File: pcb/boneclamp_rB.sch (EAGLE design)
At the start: 65 parts, among them IC1 24C, U1 AD7656YSTZ, U2 AD5754RBREZ, U3 SN74ABT541BDW, U4 ADP3303ARZ-5, U5 ADP3303ARZ-5, U6 ADR431BRZ, U7 AD7682BCPZ

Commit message: More changes to circuit
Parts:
- removed U$26: LM1085, boneclamp:LM1085
- removed U$28: SCREW3, boneclamp:SCREW3
- added C21: 0.1uF, rcl:C-EUC0603
- added C25, C28: 10uF, rcl:C-USC1206
- added U8: TPS63700DRCT, ti-extended:TPS63700DRCT
- C19, C20: value 10uF -> 0.1uF; device rcl:C-USC1206 -> rcl:C-EUC0603
- U2: value AD5754RBREZ -> ADP3303ARZ-5; device analog-devices-01:AD5754RBREZ -> analog-devices-01:ADP3303ARZ-5
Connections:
- removed net +12V: C19.1, U$26.IN
- removed net -12V: U$28.P$3
- removed net PGND: U$28.P$2
- new net AVSS: C20.1, C21.1, C28.1, U2.OUT, U2.OUT_2
- new net N$26: C20.2, U2.NR
- net AGND: now also C19.2, C21.2, C25.2, C28.2, U2.GND
- net BB_5V: now also C19.1, C25.1, U2.IN, U2.IN_2, U2.~SD
- net DAC_A: no longer U2.VOUTA
- net DAC_B: no longer U2.VOUTB
- net DAC_C: no longer U2.VOUTC
- net DAC_D: no longer U2.VOUTD
- net DGND: no longer C19.2, C20.2, U$26.ADJ
- net DVCC: no longer U2.DVCC
- net N$24: no longer U2.REFIN/REFOUT
- net N$7: no longer U2.SDO
- net N$8: no longer U2.SDIN
- net VDD: no longer U2.AVDD
- net VDD_BB: no longer C20.1, U$26.OUT
- net VSS: no longer U2.AVSS
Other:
- moved on the sheet: C19, C20, JP4, SJ1, SJ2, SJ3, SJ4, U$42

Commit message: Worked a bit on the schematic
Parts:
- removed C23: 10uF, rcl:C-USC1206
- removed C24, C26, C27: 0.1uF, rcl:C-EUC0603
- removed JP5: (no value), jumper:JP2E
- removed JP6: (no value), jumper:JP1E
- removed TP5: TPB1,27, testpad:TPB1,27
- removed U3: SN74ABT541BDW, ti-extended:SN74ABT541BDW
- removed U6: ADR431BRZ, analog-devices-01:ADR431BRZ
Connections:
- removed net N$23: JP6.1
- removed net N$25: C26.1, U6.TP_2
- removed net VDD: C23.1, C24.1, U6.VIN
- removed net VREF_OUT: C27.1, JP5.3, JP6.2, TP5.TP, U6.VOUT
- net AGND: no longer C23.2, C24.2, C26.2, U6.GND
- net VREF_2.5V: no longer JP5.2
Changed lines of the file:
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@@
 <part name="U$1" library="adafruit" deviceset="BEAGLEBONE_OUTLINE" device=""/>
 <part name="U1" library="analog-devices-01" deviceset="AD7656YSTZ" device=""/>
-<part name="U3" library="ti-extended" deviceset="SN74ABT541BDW" device=""/>
 <part name="BCIO" library="adafruit" deviceset="F15-SHEILD" device=""/>
 <part name="JP1" library="jumper" deviceset="JP1E" device=""/>
@@
 <part name="SUPPLY1" library="supply2" deviceset="AGND" device=""/>
 <part name="DGND" library="supply2" deviceset="PE" device="" value="DGND"/>
-<part name="SUPPLY3" library="supply2" deviceset="0V" device="" value="PGND"/>
 <part name="SUPPLY4" library="supply2" deviceset="AGND" device=""/>
 <part name="SUPPLY5" library="supply2" deviceset="AGND" device=""/>
@@
 <part name="JP4" library="jumper" deviceset="JP1E" device=""/>
 <part name="U$45" library="boneclamp" deviceset="V_SIG" device=""/>
-<part name="U6" library="analog-devices-01" deviceset="ADR431BRZ" device=""/>
-<part name="C24" library="rcl" deviceset="C-EU" device="C0603" value="0.1uF"/>
-<part name="SUPPLY20" library="supply2" deviceset="AGND" device=""/>
-<part name="C26" library="rcl" deviceset="C-EU" device="C0603" value="0.1uF"/>
-<part name="C27" library="rcl" deviceset="C-EU" device="C0603" value="0.1uF"/>
-<part name="SUPPLY21" library="supply2" deviceset="AGND" device=""/>
 <part name="C5" library="rcl" deviceset="C-US" device="C1206" value="10uF"/>
 <part name="C8" library="rcl" deviceset="C-US" device="C1206" value="10uF"/>
 <part name="C10" library="rcl" deviceset="C-US" device="C1206" value="10uF"/>
 <part name="C13" library="rcl" deviceset="C-US" device="C1206" value="10uF"/>
-<part name="C23" library="rcl" deviceset="C-US" device="C1206" value="10uF"/>
-<part name="U$46" library="boneclamp" deviceset="V_SIG" device=""/>
-<part name="U$47" library="boneclamp" deviceset="V_SIG" device=""/>
-<part name="TP5" library="testpad" deviceset="TP" device="B1,27"/>
-<part name="JP5" library="jumper" deviceset="JP2E" device=""/>
-<part name="JP6" library="jumper" deviceset="JP1E" device=""/>
 <part name="U$42" library="analog-devices-02" deviceset="AD5686RARUZ" device=""/>
 <part name="U7" library="analog-devices-02" deviceset="AD7682BCPZ" device=""/>
@@
 <instances>
 <instance part="U$1" gate="G$1" x="-35.56" y="48.26"/>
-<instance part="U3" gate="A" x="48.26" y="53.34"/>
 <instance part="DGND2" gate="PE" x="2.54" y="-20.32"/>
 <instance part="SUPPLY8" gate="G$1" x="10.16" y="-20.32"/>
@@
 <instance part="SUPPLY1" gate="G$1" x="-81.28" y="45.72"/>
 <instance part="DGND" gate="PE" x="25.4" y="-33.02"/>
-<instance part="SUPPLY3" gate="0V" x="30.48" y="-58.42"/>
 <instance part="SUPPLY4" gate="G$1" x="-10.16" y="-22.86"/>
 <instance part="SUPPLY5" gate="G$1" x="0" y="-22.86"/>
@@
 </segment>
 </net>
-</nets>
-</sheet>
-<sheet>
-<description>REFERENCES</description>
-<plain>
-</plain>
-<instances>
-<instance part="U6" gate="A" x="0" y="0"/>
-<instance part="C24" gate="G$1" x="-48.26" y="-2.54"/>
-<instance part="SUPPLY20" gate="G$1" x="-48.26" y="-22.86"/>
-<instance part="C26" gate="G$1" x="-33.02" y="-2.54"/>
-<instance part="C27" gate="G$1" x="33.02" y="-2.54"/>
-<instance part="SUPPLY21" gate="G$1" x="33.02" y="-22.86"/>
-<instance part="C23" gate="G$1" x="-60.96" y="-2.54"/>
-<instance part="U$46" gate="G$1" x="116.84" y="0"/>
-<instance part="U$47" gate="G$1" x="-73.66" y="7.62" rot="R180"/>
-<instance part="TP5" gate="G$1" x="33.02" y="10.16"/>
-<instance part="JP5" gate="1" x="91.44" y="0" rot="R90"/>
-<instance part="JP6" gate="A" x="71.12" y="-2.54" rot="R90"/>
-</instances>
-<busses>
-</busses>
-<nets>
-<net name="AGND" class="0">
-<segment>
-<pinref part="U6" gate="A" pin="GND"/>
-<wire x1="-17.78" y1="-15.24" x2="-33.02" y2="-15.24" width="0.1524" layer="91"/>
-<wire x1="-33.02" y1="-15.24" x2="-48.26" y2="-15.24" width="0.1524" layer="91"/>
-<wire x1="-48.26" y1="-15.24" x2="-60.96" y2="-15.24" width="0.1524" layer="91"/>
-<wire x1="-60.96" y1="-15.24" x2="-60.96" y2="-7.62" width="0.1524" layer="91"/>
-<pinref part="C24" gate="G$1" pin="2"/>
-<wire x1="-48.26" y1="-7.62" x2="-48.26" y2="-15.24" width="0.1524" layer="91"/>
-<junction x="-48.26" y="-15.24"/>
-<wire x1="-48.26" y1="-15.24" x2="-48.26" y2="-20.32" width="0.1524" layer="91"/>
-<pinref part="SUPPLY20" gate="G$1" pin="AGND"/>
-<pinref part="C26" gate="G$1" pin="2"/>
-<wire x1="-33.02" y1="-7.62" x2="-33.02" y2="-15.24" width="0.1524" layer="91"/>
-<junction x="-33.02" y="-15.24"/>
-<pinref part="C23" gate="G$1" pin="2"/>
-</segment>
-<segment>
-<wire x1="33.02" y1="-7.62" x2="33.02" y2="-20.32" width="0.1524" layer="91"/>
-<pinref part="SUPPLY21" gate="G$1" pin="AGND"/>
-</segment>
-</net>
-<net name="VDD" class="0">
-<segment>
-<pinref part="U6" gate="A" pin="VIN"/>
-<wire x1="-17.78" y1="7.62" x2="-48.26" y2="7.62" width="0.1524" layer="91"/>
-<wire x1="-48.26" y1="7.62" x2="-60.96" y2="7.62" width="0.1524" layer="91"/>
-<wire x1="-60.96" y1="7.62" x2="-73.66" y2="7.62" width="0.1524" layer="91"/>
-<wire x1="-60.96" y1="0" x2="-60.96" y2="7.62" width="0.1524" layer="91"/>
-<junction x="-60.96" y="7.62"/>
-<pinref part="C24" gate="G$1" pin="1"/>
-<wire x1="-48.26" y1="0" x2="-48.26" y2="7.62" width="0.1524" layer="91"/>
-<junction x="-48.26" y="7.62"/>
-<pinref part="C23" gate="G$1" pin="1"/>
-<label x="-80.01" y="6.985" size="1.778" layer="95"/>
-</segment>
-</net>
-<net name="N$25" class="0">
-<segment>
-<pinref part="U6" gate="A" pin="TP_2"/>
-<wire x1="-17.78" y1="-5.08" x2="-22.86" y2="-5.08" width="0.1524" layer="91"/>
-<wire x1="-22.86" y1="-5.08" x2="-22.86" y2="2.54" width="0.1524" layer="91"/>
-<wire x1="-22.86" y1="2.54" x2="-33.02" y2="2.54" width="0.1524" layer="91"/>
-<pinref part="C26" gate="G$1" pin="1"/>
-<wire x1="-33.02" y1="2.54" x2="-33.02" y2="0" width="0.1524" layer="91"/>
-</segment>
-</net>
-<net name="VREF_2.5V" class="0">
-<segment>
-<pinref part="JP5" gate="1" pin="2"/>
-<wire x1="93.98" y1="0" x2="116.84" y2="0" width="0.1524" layer="91"/>
-<label x="118.11" y="-0.635" size="1.778" layer="95"/>
-</segment>
-</net>
-<net name="VREF_OUT" class="0">
-<segment>
-<pinref part="U6" gate="A" pin="VOUT"/>
-<wire x1="17.78" y1="7.62" x2="33.02" y2="7.62" width="0.1524" layer="91"/>
-<pinref part="C27" gate="G$1" pin="1"/>
-<wire x1="33.02" y1="0" x2="33.02" y2="7.62" width="0.1524" layer="91"/>
-<junction x="33.02" y="7.62"/>
-<pinref part="TP5" gate="G$1" pin="TP"/>
-<pinref part="JP5" gate="1" pin="3"/>
-<wire x1="93.98" y1="2.54" x2="101.6" y2="2.54" width="0.1524" layer="91"/>
-<wire x1="101.6" y1="2.54" x2="101.6" y2="7.62" width="0.1524" layer="91"/>
-<wire x1="101.6" y1="7.62" x2="73.66" y2="7.62" width="0.1524" layer="91"/>
-<pinref part="JP6" gate="A" pin="2"/>
-<wire x1="73.66" y1="7.62" x2="33.02" y2="7.62" width="0.1524" layer="91"/>
-<wire x1="73.66" y1="0" x2="73.66" y2="7.62" width="0.1524" layer="91"/>
-<junction x="73.66" y="7.62"/>
-</segment>
-</net>
-<net name="N$23" class="0">
-<segment>
-<pinref part="JP6" gate="A" pin="1"/>
-<wire x1="73.66" y1="-2.54" x2="73.66" y2="-35.56" width="0.1524" layer="91"/>
-<wire x1="73.66" y1="-35.56" x2="81.28" y2="-35.56" width="0.1524" layer="91"/>
-</segment>
-</net>

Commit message: Wired the DC-DC inverter
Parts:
- added C23: 10uF, rcl:C-EUC0805
- added C24: 22nF, rcl:C-EUC0805
- added C26: 0.1uF, rcl:C-EUC0805
- added C27: 4.7nF, rcl:C-EUC0805
- added C29: 10nF, rcl:C-EUC0805
- added C30, C31, C32, C33: 4.7uF, rcl:C-EUC0805
- added C34: 0.22uF, rcl:C-EUC0805
- added C35: 10pF, rcl:C-EUC0805
- added R12: 750, resistor:R-US_R0805
- added R13: 150k, resistor:R-US_R0805
- added R5: 100k, resistor:R-US_R0805
- added U$27: SCHOTTKY-DIODE-2, boneclamp:SCHOTTKY-DIODE-2
- added U$28: 4.7uH, boneclamp:L-US
- C15, C16, C17, C18: device rcl:C-EUC0603 -> rcl:C-EUC0805
- R1, R2, R3, R4: device rcl:R-US_R0603 -> rcl:R-US_R0805
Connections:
- removed net VDD_BB: U$1.VDD_5V@1, U$1.VDD_5V@2
- new net N$23: C26.1, R5.2, U8.EN, U8.VIN
- new net N$25: C27.1, U8.COMP
- new net N$27: U$27.A, U$28.1, U8.SW
- new net N$30: C35.1, R12.2, R13.1, U8.FB
- new net N$31: C34.1, R13.2, U8.VREF
- new net VDD_5V: C23.1, C24.1, R5.1, U$1.VDD_5V@1, U$1.VDD_5V@2, U8.IN
- new net _VSS: C29.1, C30.1, C31.1, C32.1, C33.1, C35.2, R12.1, U$27.C, U8.OUT
- net AGND: now also C23.2, C24.2, C26.2, C27.2, C29.2, C30.2, C31.2, C32.2, C33.2, C34.2, U$28.2, U8.EP, U8.GND, U8.PS_GND
- net BB_5V: no longer U$1.SYS_5V@1, U$1.SYS_5V@2
- net DAC_A: now also C15.1, R1.2, TP4.TP; no longer C18.1, R4.2, TP1.TP
- net DAC_B: now also C16.1, R2.2, TP3.TP; no longer C17.1, R3.2, TP2.TP
- net DAC_C: now also C17.1, R3.2, TP2.TP; no longer C16.1, R2.2, TP3.TP
- net DAC_D: now also C18.1, R4.2, TP1.TP; no longer C15.1, R1.2, TP4.TP

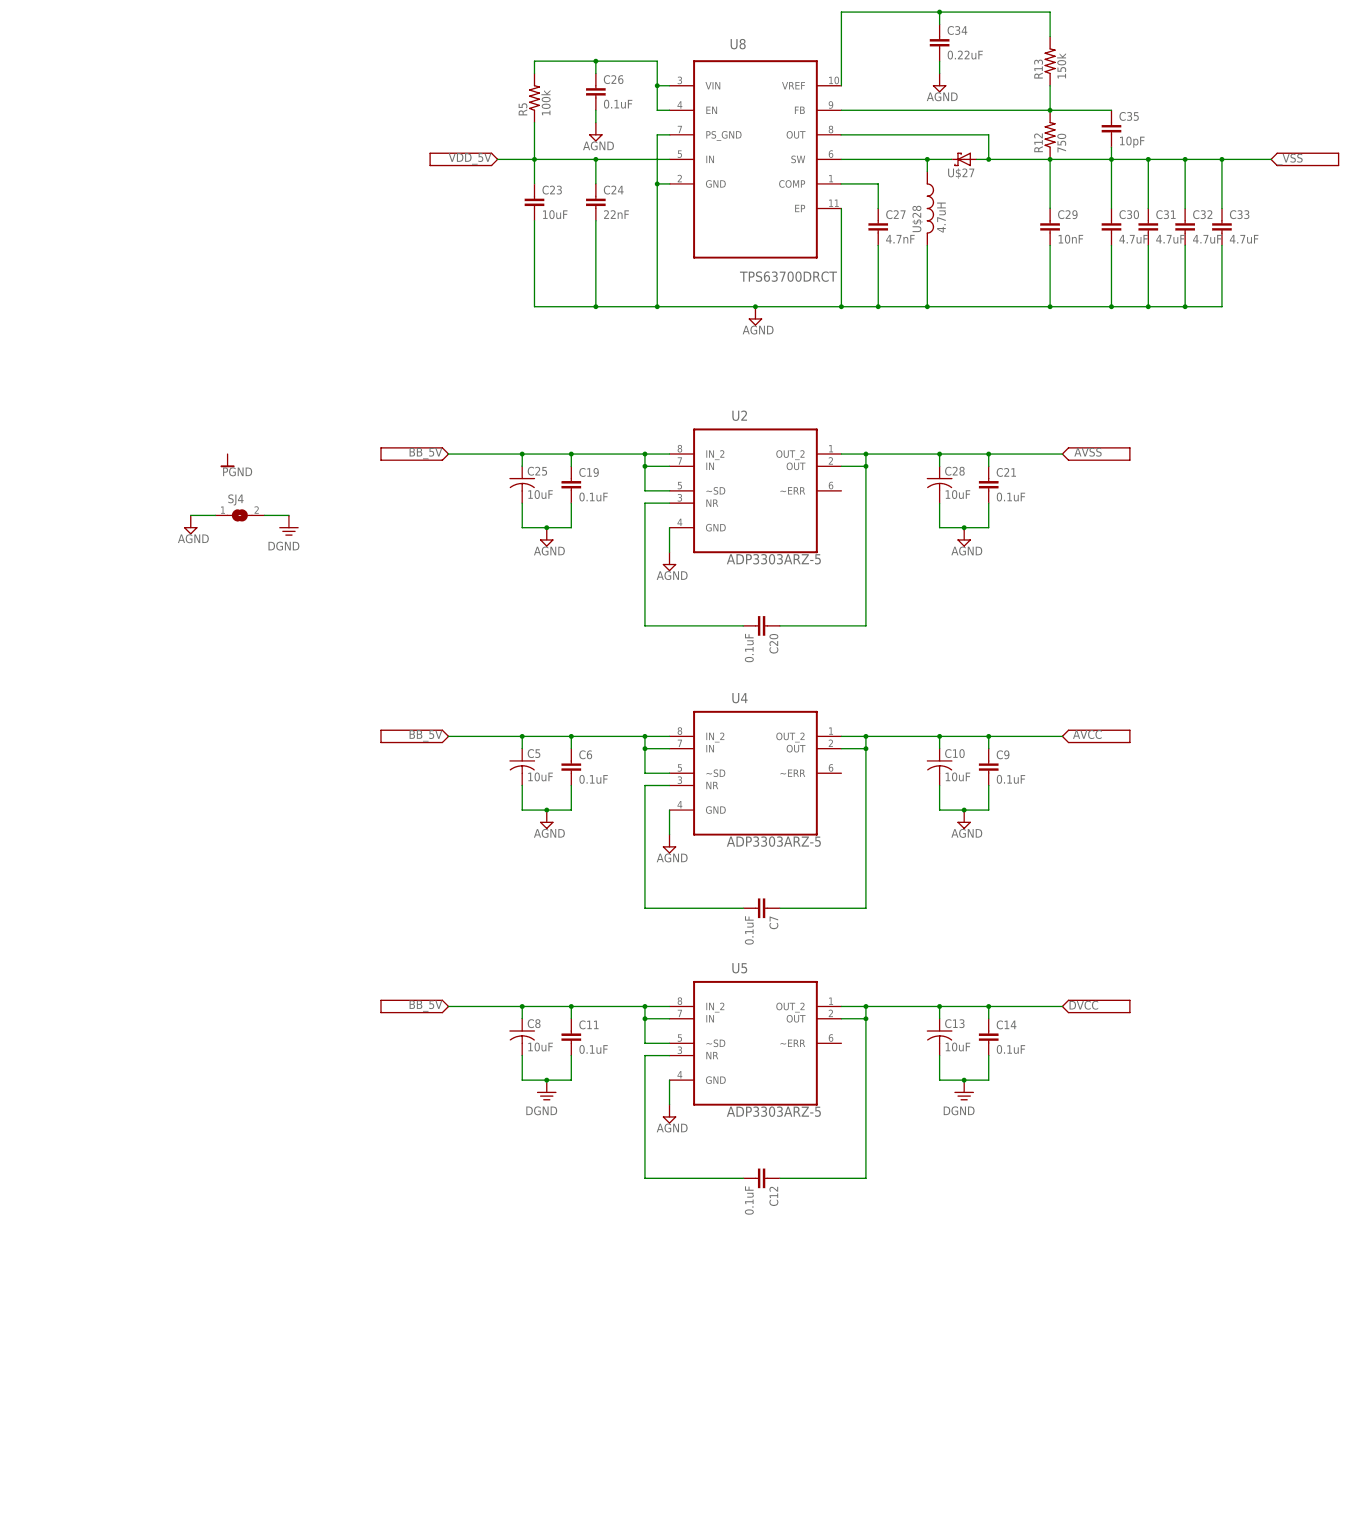
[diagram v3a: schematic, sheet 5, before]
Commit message: Added negative LDO regulator
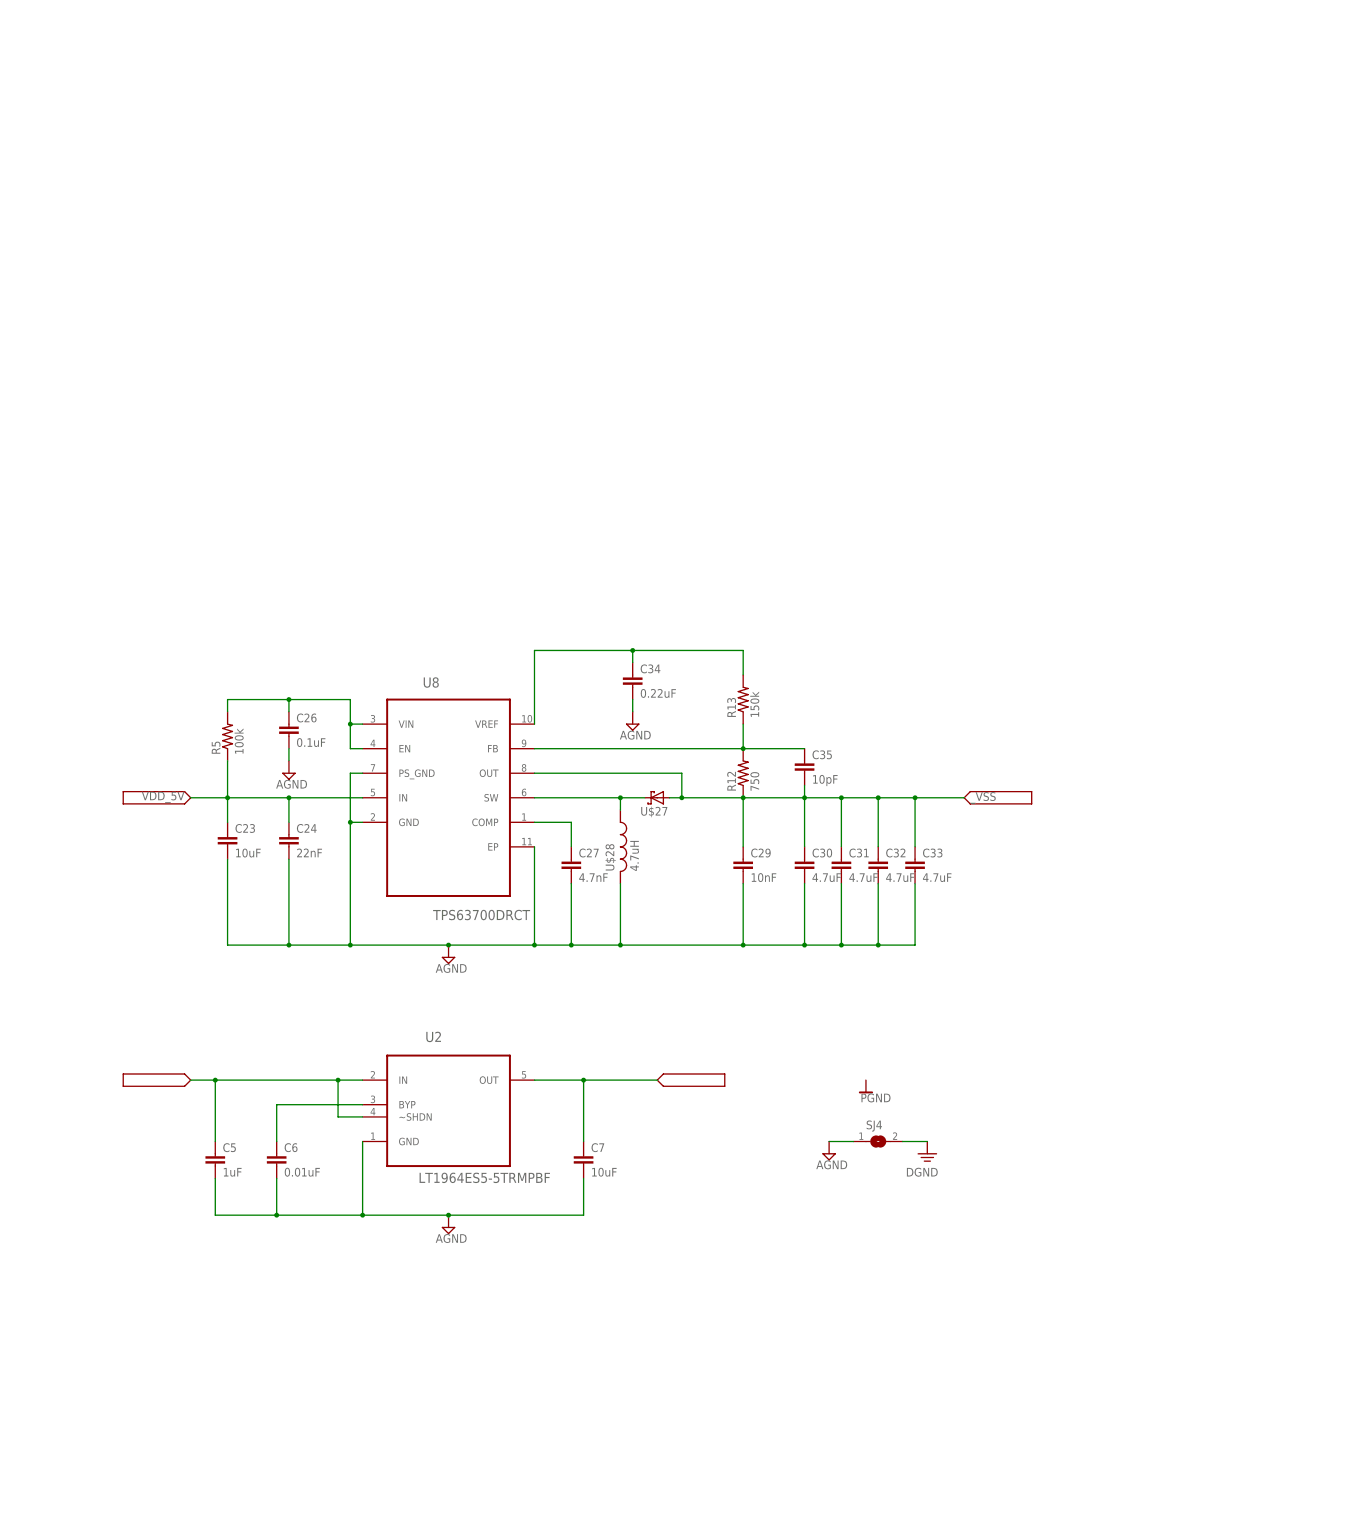
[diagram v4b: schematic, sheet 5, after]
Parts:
- removed C10, C13, C25, C28, C8: 10uF, rcl:C-USC1206
- removed C11, C12, C14, C19, C20, C21, C9: 0.1uF, rcl:C-EUC0603
- removed U4, U5: ADP3303ARZ-5, analog-devices-01:ADP3303ARZ-5
- C5: value 10uF -> 1uF; device rcl:C-USC1206 -> rcl:C-EUC0805
- C6: value 0.1uF -> 0.01uF; device rcl:C-EUC0603 -> rcl:C-EUC0805
- C7: value 0.1uF -> 10uF; device rcl:C-EUC0603 -> rcl:C-EUC0805
- U2: value ADP3303ARZ-5 -> LT1964ES5-5TRMPBF; device analog-devices-01:ADP3303ARZ-5 -> linear-extended-01:LT1964ES5-5TRMPBF
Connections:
- removed net AVCC: C10.1, C7.1, C9.1, U4.OUT, U4.OUT_2
- removed net AVSS: C20.1, C21.1, C28.1, U2.OUT, U2.OUT_2
- removed net BB_5V: C11.1, C19.1, C25.1, C5.1, C6.1, C8.1, U2.IN, U2.IN_2, U2.~SD, U4.IN, U4.IN_2, U4.~SD, U5.IN, U5.IN_2, U5.~SD
- removed net DVCC: C12.1, C13.1, C14.1, U5.OUT, U5.OUT_2
- removed net N$15: C12.2, U5.NR
- removed net N$26: C20.2, U2.NR
- new net VDD: U$42.VDD
- net AGND: now also C7.2; no longer C10.2, C19.2, C21.2, C25.2, C28.2, C9.2, U4.GND, U5.GND
- net DAC_A: now also U$42.VOUTA
- net DAC_B: now also U$42.VOUTB
- net DAC_C: now also U$42.VOUTC
- net DAC_D: now also U$42.VOUTD
- net DGND: no longer C11.2, C13.2, C14.2, C8.2
- net N$16: now also C6.1, U2.BYP; no longer C7.2, U4.NR
- net N$24: now also U$42.VREF
- net N$7: now also U$42.SDO
- net N$8: now also U$42.SDIN
- net VDRIVE: now also U$42.VDRIVE
- net VSS: now also C7.1, U2.OUT
- net _VSS: now also C5.1, U2.IN, U2.~SHDN
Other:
- moved on the sheet: C15, C16, C17, C18, C23, C24, C26, C27, C29, C30, C31, C32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

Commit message: Minor schematic edit
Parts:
- added U3: LT1962EMS8-5PBF, linear-extended-01:LT1962EMS8-5PBF
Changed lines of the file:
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@@
 <part name="C7" library="rcl" deviceset="C-EU" device="C0805" value="10uF"/>
 <part name="U$20" library="boneclamp" deviceset="V_SIG" device=""/>
+<part name="U3" library="linear-extended-01" deviceset="LT1962EMS8-5PBF" device=""/>
 </parts>
 <sheets>
@@
 <instance part="C7" gate="G$1" x="27.94" y="-12.7"/>
 <instance part="U$20" gate="G$1" x="43.18" y="2.54"/>
+<instance part="U3" gate="A" x="0" y="-63.5"/>
 </instances>
 <busses>
